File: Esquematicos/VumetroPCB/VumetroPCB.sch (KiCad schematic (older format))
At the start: 16 parts, among them J1 AudioJack, U1 conn_teclado_4x4, U2 opa2350pa, U3 MAX7219, U4 MatrixLed8x8

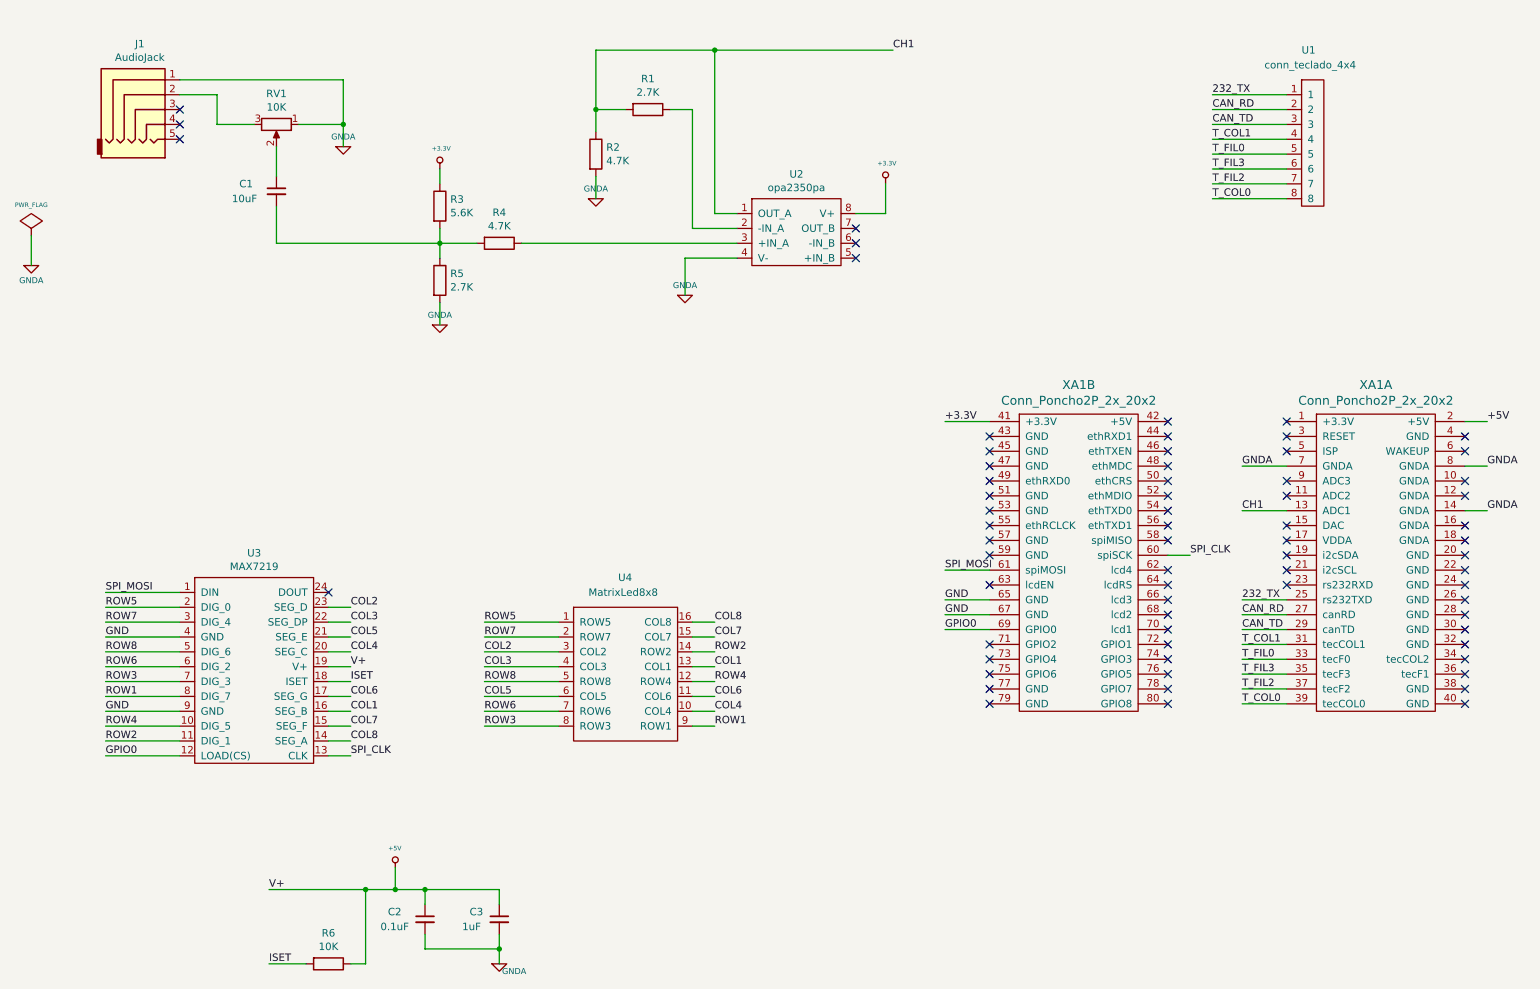
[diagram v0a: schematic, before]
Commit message: Cambiar la huella del potenciometro Bourns3296
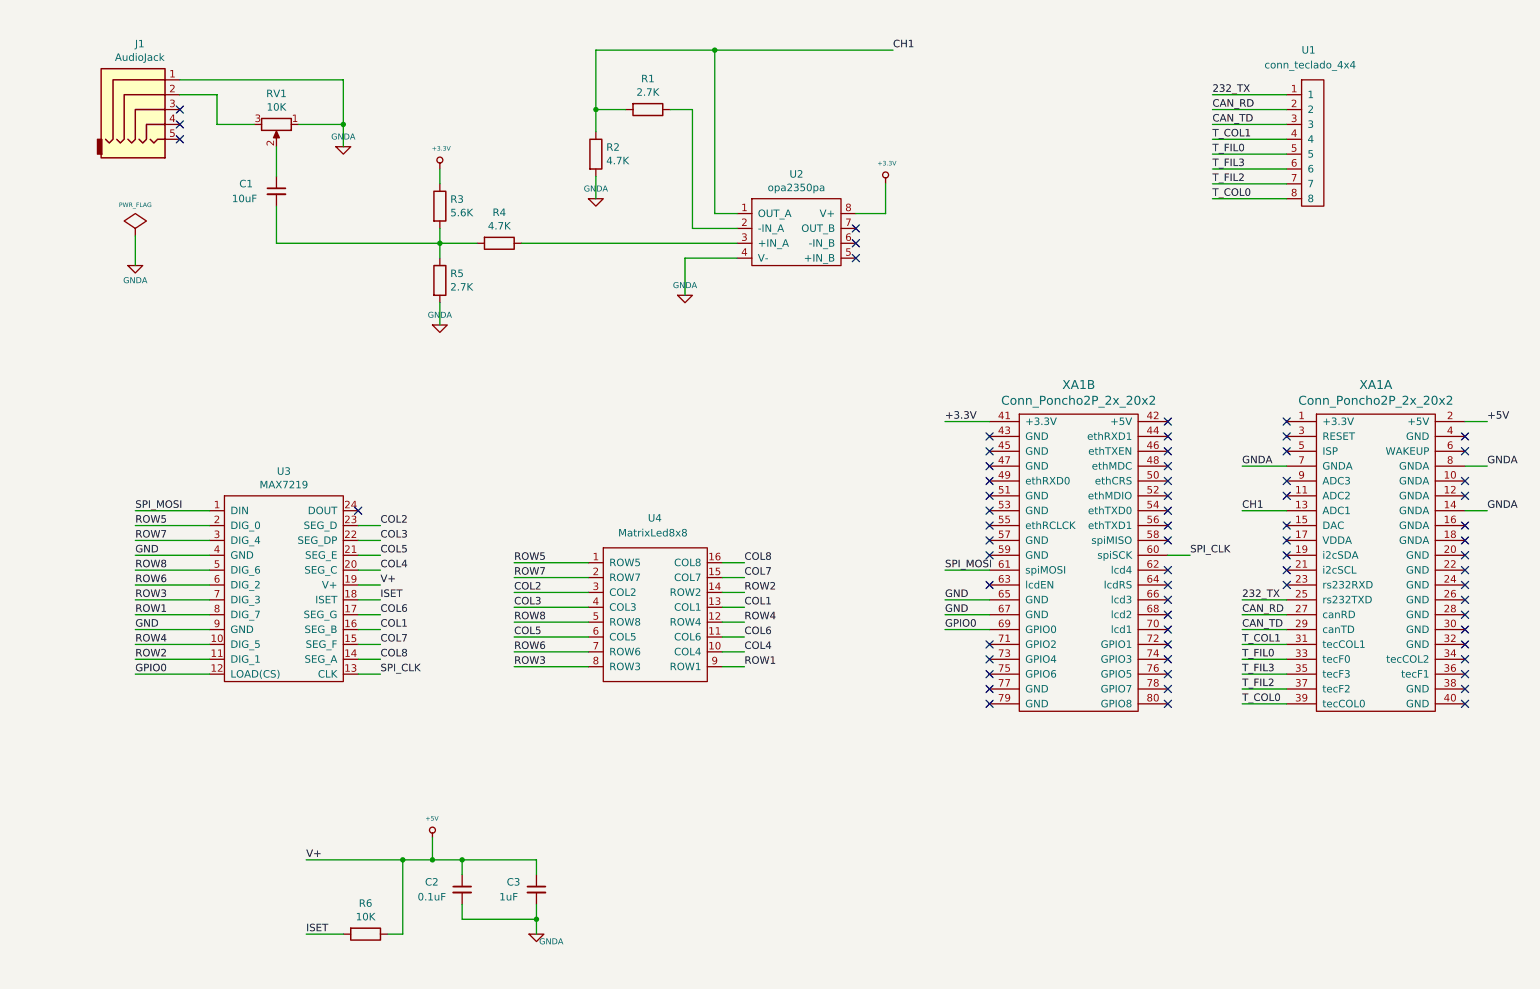
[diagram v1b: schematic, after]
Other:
- moved on the sheet: C2, C3, R6, U3, U4

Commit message: Correcciones al diseño del PCB.
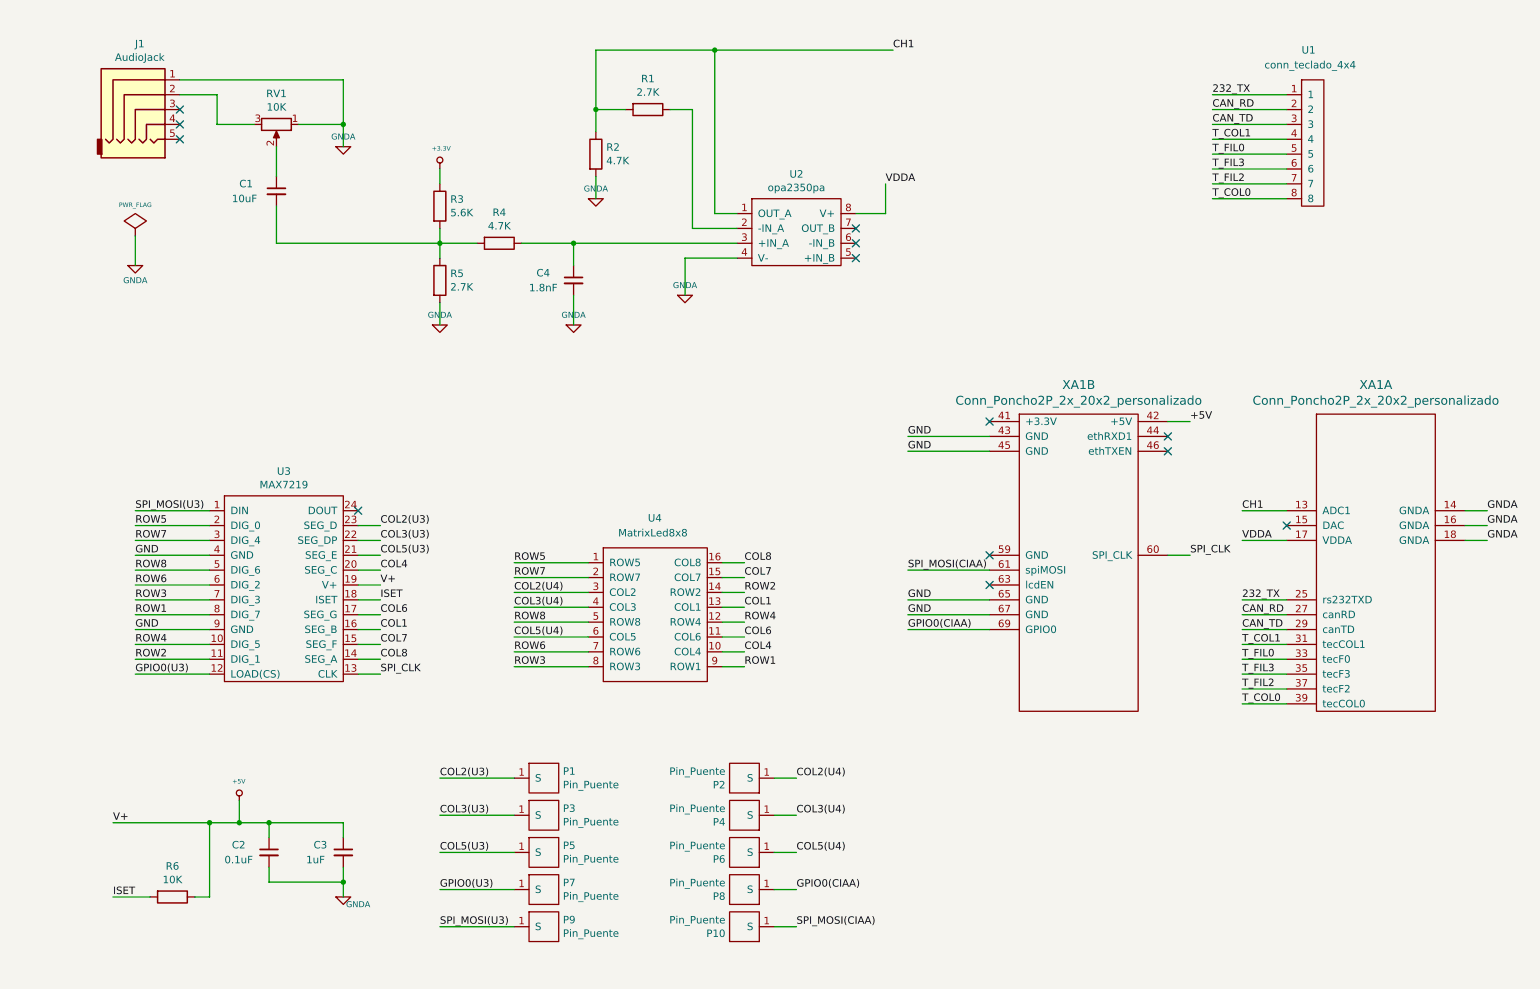
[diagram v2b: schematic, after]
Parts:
- removed XA1: Conn_Poncho2P_2x_20x2, Projecto:Conn_Poncho_Personalizado, symbol Poncho_Esqueleto:Conn_Poncho2P_2x_20x2
- added C4: 1.8nF, Projecto:Capacitor_Disco, symbol vumetro:C
- added P1, P10, P2, P3, P4, P5, P6, P7, P8, P9: Pin_Puente, Projecto:Pin_Puente, symbol vumetro:Pin_Puente
- added XA1: Conn_Poncho2P_2x_20x2_personalizado, Projecto:Conn_Poncho_Personalizado, symbol vumetro:Conn_Poncho2P_2x_20x2_personalizado
- C2: footprint Projecto:Capacitor -> Projecto:Capacitor_Disco
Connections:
- net +3.3V: no longer U2.8 (V+)
- net +5V: now also XA1.42 (+5V)
- net 232_TX: now also XA1.25 (rs232TXD)
- net CAN_RD: now also XA1.27 (canRD)
- net CAN_TD: now also XA1.29 (canTD)
- net CH1: now also XA1.13 (ADC1)
- net GND: now also XA1.43 (GND), XA1.45 (GND), XA1.65 (GND), XA1.67 (GND)
- net GNDA: now also C4.2, XA1.14 (GNDA), XA1.16 (GNDA), XA1.18 (GNDA)
- net SPI_CLK: now also XA1.60 (SPI_CLK)
- net T_COL0: now also XA1.39 (tecCOL0)
- net T_COL1: now also XA1.31 (tecCOL1)
- net T_FIL0: now also XA1.33 (tecF0)
- net T_FIL2: now also XA1.37 (tecF2)
- net T_FIL3: now also XA1.35 (tecF3)
- net at R4.1, U2.3 (+IN_A): now also C4.1
- net COL2 renamed COL2(U3)
- net COL2(U3): now also P1.1 (S); no longer U4.3 (COL2)
- net COL3 renamed COL3(U3)
- net COL3(U3): now also P3.1 (S); no longer U4.4 (COL3)
- net COL5 renamed COL5(U3)
- net COL5(U3): now also P5.1 (S); no longer U4.6 (COL5)
- net GPIO0 renamed GPIO0(U3)
- net GPIO0(U3): now also P7.1 (S)
- net SPI_MOSI renamed SPI_MOSI(U3)
- net SPI_MOSI(U3): now also P9.1 (S)
- new net COL2(U4): P2.1 (S), U4.3 (COL2)
- new net COL3(U4): P4.1 (S), U4.4 (COL3)
- new net COL5(U4): P6.1 (S), U4.6 (COL5)
- new net GPIO0(CIAA): P8.1 (S), XA1.69 (GPIO0)
- new net SPI_MOSI(CIAA): P10.1 (S), XA1.61 (spiMOSI)
- new net VDDA: U2.8 (V+), XA1.17 (VDDA)
- no-connect marks 68 -> 13
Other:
- moved on the sheet: C2, C3, R6

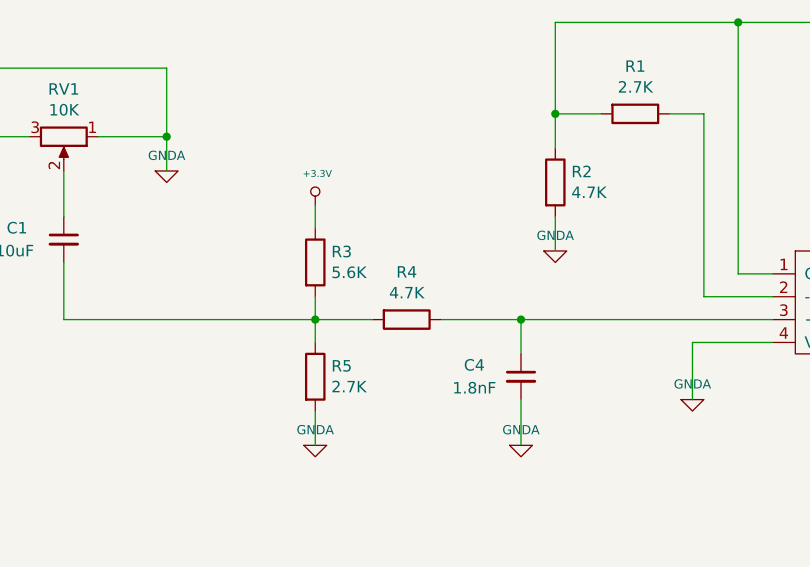
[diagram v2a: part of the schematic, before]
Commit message: Arreglar la conexión de la resistencia R3
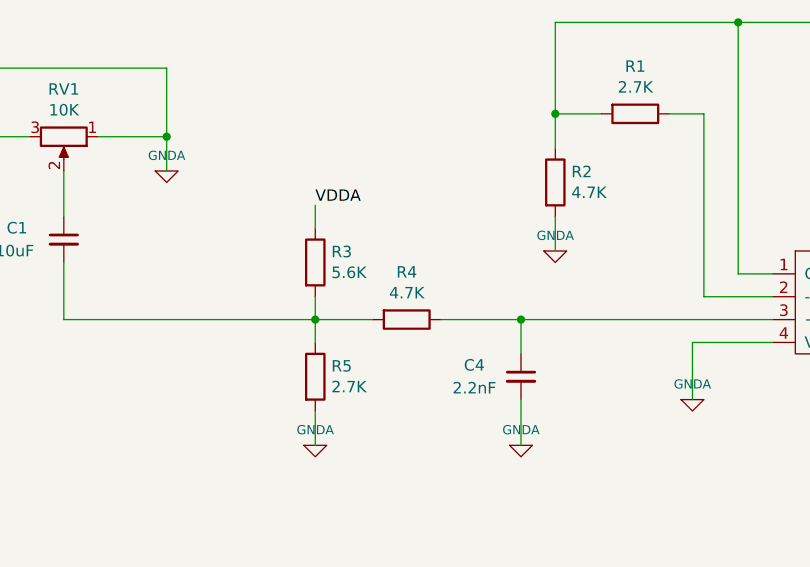
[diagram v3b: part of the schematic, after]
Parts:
- C4: value 1.8nF -> 2.2nF
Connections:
- net +3.3V is gone; now on net VDDA: R3.1
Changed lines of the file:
@@
-$EndComp
-$Comp
-L Misc_Poncho_Grande:+3.3V #PWR0108
-U 1 1 5BFE2CAB
-P 3450 2050
-F 0 "#PWR0108" H 3450 2010 30  0001 C CNN
-F 1 "+3.3V" H 3459 2188 30  0000 C CNN
-F 2 "" H 3450 2050 60  0000 C CNN
-F 3 "" H 3450 2050 60  0000 C CNN
-	1    3450 2050
-	1    0    0    -1
 $EndComp
 $Comp
@@
 P 4350 2800
 F 0 "C4" H 4100 2850 50  0000 L CNN
-F 1 "1.8nF" H 4050 2750 50  0000 L CNN
+F 1 "2.2nF" H 4050 2750 50  0000 L CNN
 F 2 "Projecto:Capacitor_Disco" H 4350 2800 50  0001 C CNN
 F 3 "~" H 4350 2800 50  0001 C CNN
@@
 Text Label 5850 7150 0    50   ~ 0
 SPI_MOSI(CIAA)
+Text Label 3450 2050 0    50   ~ 0
+VDDA
 $EndSCHEMATC

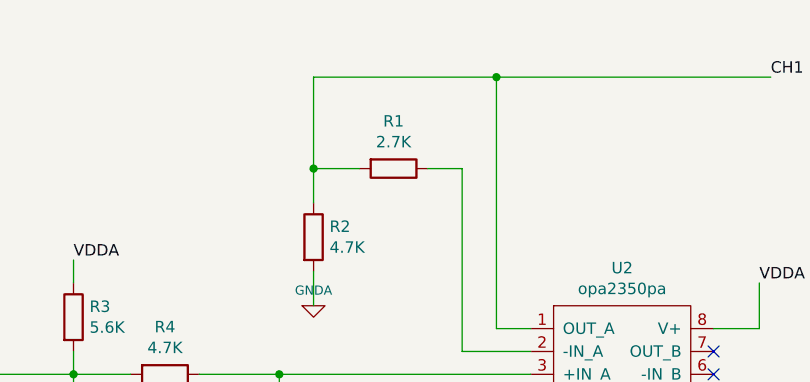
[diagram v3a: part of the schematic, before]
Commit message: Arreglo de los errores de diseño en la PCB
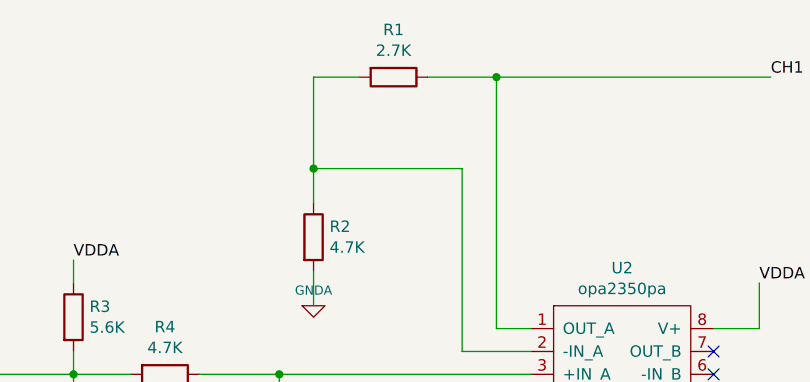
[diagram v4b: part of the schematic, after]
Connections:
- net CH1: now also R1.1; no longer R1.2, R2.1
- net at U2.2 (-IN_A): now also R1.2, R2.1; no longer R1.1
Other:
- moved on the sheet: R1
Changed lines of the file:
@@
 L vumetro:R R1
 U 1 1 5C141C3A
-P 4850 1650
-F 0 "R1" V 4643 1650 50  0000 C CNN
-F 1 "2.7K" V 4734 1650 50  0000 C CNN
-F 2 "Projecto:Resistor" V 4780 1650 50  0001 C CNN
-F 3 "~" H 4850 1650 50  0001 C CNN
-	1    4850 1650
+P 4850 1250
+F 0 "R1" V 4643 1250 50  0000 C CNN
+F 1 "2.7K" V 4734 1250 50  0000 C CNN
+F 2 "Projecto:Resistor" V 4780 1250 50  0001 C CNN
+F 3 "~" H 4850 1250 50  0001 C CNN
+	1    4850 1250
 	0    1    1    0
 $EndComp
@@
 	4500 1800 4500 1650
 Wire Wire Line
-	4500 1250 5300 1250
-Wire Wire Line
-	4700 1650 4500 1650
+	4500 1250 4700 1250
 Connection ~ 4500 1650
 Wire Wire Line
 	4500 1650 4500 1250
-Wire Wire Line
-	5000 1650 5150 1650
 Wire Wire Line
 	4500 2100 4500 2250
@@
 Text Label 3450 2050 0    50   ~ 0
 VDDA
+Wire Wire Line
+	5000 1250 5300 1250
+Wire Wire Line
+	4500 1650 5150 1650
 $EndSCHEMATC
